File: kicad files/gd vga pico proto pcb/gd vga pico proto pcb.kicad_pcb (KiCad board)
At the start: 2 copper layers, 0 parts

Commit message: floor planning complete
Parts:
- added C1: 10u, Capacitor_SMD:C_0805_2012Metric, F.Cu at (88.2, 95.9)
- added C2: 1u, Capacitor_SMD:C_0805_2012Metric, B.Cu at (104.6, 79.2)
- added C3: 1u, Capacitor_SMD:C_0805_2012Metric, B.Cu at (103.1, 57.1)
- added C4: 1u, Capacitor_SMD:C_0805_2012Metric, B.Cu at (103.0, 68.7)
- added J1: RGB Bin, Connector_PinSocket_2.54mm:PinSocket_2x04_P2.54mm_Vertical, F.Cu at (80.1, 93.1)
- added J2: CLKS, Connector_PinSocket_2.54mm:PinSocket_2x04_P2.54mm_Vertical, F.Cu at (80.1, 49.6)
- added J3: Conn_01x05, Connector_PinHeader_2.54mm:PinHeader_1x05_P2.54mm_Vertical, F.Cu at (99.3, 46.1)
- added J4: L77HDE15SD1CH4F, Connector_Dsub:DSUB-15-HD_Female_Horizontal_P2.29x1.98mm_EdgePinOffset8.35mm_Housed_MountingHolesOffset10.89mm, F.Cu at (126.2, 68.7)
- added J5: VID_TXRX, Connector_PinHeader_2.54mm:PinHeader_1x04_P2.54mm_Vertical, F.Cu at (117.9, 64.7)
- added J6: WIN, Connector_PinHeader_2.54mm:PinHeader_1x02_P2.54mm_Vertical, F.Cu at (89.3, 79.4)
- added J7: 5V, Connector_PinSocket_2.54mm:PinSocket_1x04_P2.54mm_Vertical, F.Cu at (80.1, 63.4)
- added JP1: 14M, Jumper:SolderJumper-2_P1.3mm_Bridged_RoundedPad1.0x1.5mm, F.Cu at (84.3, 53.6)
- added JP2: 7M, Jumper:SolderJumper-2_P1.3mm_Open_TrianglePad1.0x1.5mm, F.Cu at (92.1, 46.5)
- added R1: 100, Resistor_SMD:R_0603_1608Metric, B.Cu at (127.7, 81.3)
- added R10: 100, Resistor_SMD:R_0603_1608Metric, B.Cu at (122.1, 77.7)
- added R11: 100, Resistor_SMD:R_0603_1608Metric, B.Cu at (122.1, 81.3)
- added R2: 1k, Resistor_SMD:R_0603_1608Metric, B.Cu at (117.7, 99.9)
- added R3: 390, Resistor_SMD:R_0603_1608Metric, B.Cu at (117.6, 97.4)
- added R4: 2k2, Resistor_SMD:R_0603_1608Metric, B.Cu at (117.8, 92.3)
- added R5: 1k, Resistor_SMD:R_0603_1608Metric, B.Cu at (117.8, 89.8)
- added R6: 470, Resistor_SMD:R_0603_1608Metric, B.Cu at (117.9, 87.2)
- added R7: 2k2, Resistor_SMD:R_0603_1608Metric, B.Cu at (117.8, 84.7)
- added R8: 1k, Resistor_SMD:R_0603_1608Metric, B.Cu at (117.5, 79.6)
- added R9: 470, Resistor_SMD:R_0603_1608Metric, B.Cu at (117.6, 77.1)
- added RNP1: 4k7, Resistor_SMD:R_0603_1608Metric, B.Cu at (121.9, 65.0)
- added RNP2: 4k7, Resistor_SMD:R_0603_1608Metric, B.Cu at (122.1, 62.0)
- added SW1: RESET, My Libraries:SW_Push_CK_PTS525_SM15, F.Cu at (92.7, 105.9)
- added TP1: TestPoint_Harwin, My Libraries:Harwin-S1751-46-Test-Point, F.Cu at (88.2, 90.0)
- added TP2: TestPoint_Harwin, My Libraries:Harwin-S1751-46-Test-Point, F.Cu at (122.1, 77.7)
- added TP3: TestPoint_Harwin, My Libraries:Harwin-S1751-46-Test-Point, F.Cu at (122.1, 81.1)
- added TP4: TestPoint_Harwin, My Libraries:Harwin-S1751-46-Test-Point, F.Cu at (124.7, 49.6)
- added TP5: TestPoint_Harwin, My Libraries:Harwin-S1751-46-Test-Point, F.Cu at (128.5, 94.2)
- added TP6: TestPoint_Harwin, My Libraries:Harwin-S1751-46-Test-Point, F.Cu at (122.0, 68.8)
- added TP7: TestPoint_Harwin, My Libraries:Harwin-S1751-46-Test-Point, F.Cu at (122.0, 71.1)
- added TP8: TestPoint_Harwin, My Libraries:Harwin-S1751-46-Test-Point, F.Cu at (122.0, 73.4)
- added U1: Pico, RPi_Pico:RPi_Pico_SMD_TH, F.Cu at (103.7, 75.8)
- added U2: 74HCT245, Package_SO:SO-20_5.3x12.6mm_P1.27mm, B.Cu at (104.9, 87.8)
- added U3: 74LVC2G04, Package_TO_SOT_SMD:SOT-23-6, B.Cu at (103.1, 60.3)
- added U4: 74LVC2G04, Package_TO_SOT_SMD:SOT-23-6, B.Cu at (103.1, 64.7)
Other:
- board outline added: 66 x 66 mm

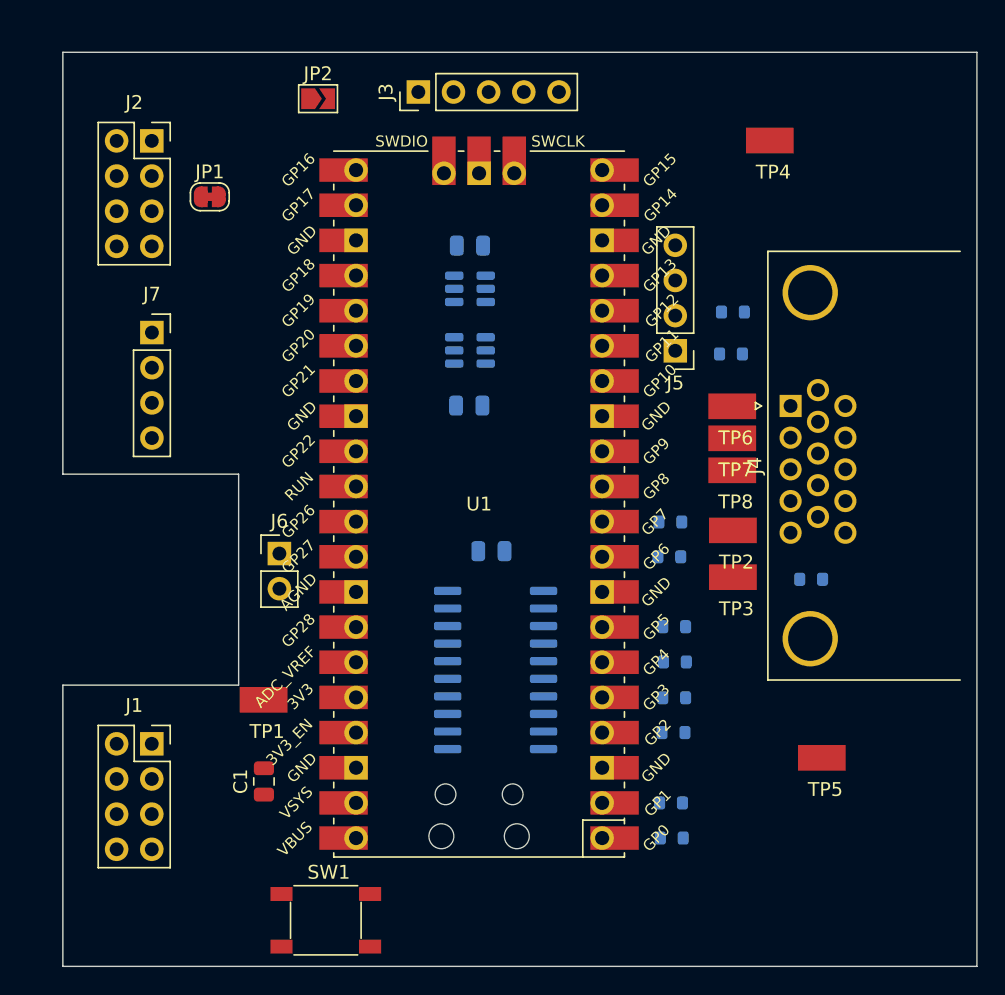
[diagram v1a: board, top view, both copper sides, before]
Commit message: swapped from pico to RP2040--yay
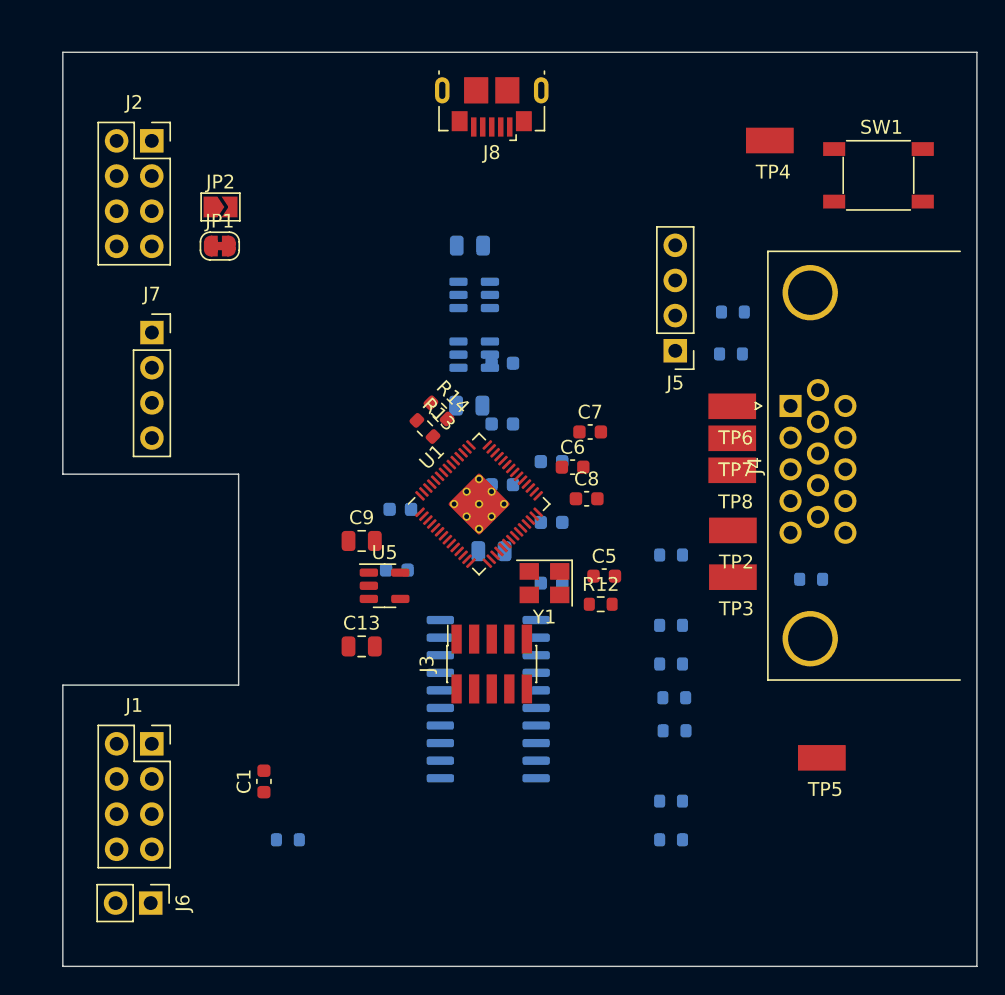
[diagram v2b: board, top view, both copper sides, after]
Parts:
- removed TP1: TestPoint_Harwin, My Libraries:Harwin-S1751-46-Test-Point
- added C10: 100n, Capacitor_SMD:C_0603_1608Metric, B.Cu at (105.4, 65.6)
- added C11: 1u, Capacitor_SMD:C_0603_1608Metric, B.Cu at (105.4, 70.0)
- added C12: 100n, Capacitor_SMD:C_0603_1608Metric, B.Cu at (105.4, 74.4)
- added C13: 1u, Capacitor_SMD:C_0805_2012Metric, F.Cu at (95.2, 86.1)
- added C14: 100n, Capacitor_SMD:C_0603_1608Metric, B.Cu at (109.0, 72.8)
- added C15: 100n, Capacitor_SMD:C_0603_1608Metric, B.Cu at (109.0, 77.1)
- added C16: 100n, Capacitor_SMD:C_0603_1608Metric, B.Cu at (109.0, 81.5)
- added C17: 100n, Capacitor_SMD:C_0603_1608Metric, B.Cu at (98.0, 76.2)
- added C18: 100n, Capacitor_SMD:C_0603_1608Metric, B.Cu at (97.8, 80.6)
- added C5: 27p, Capacitor_SMD:C_0603_1608Metric, F.Cu at (112.8, 81.0)
- added C6: 100n, Capacitor_SMD:C_0603_1608Metric, F.Cu at (110.5, 73.2)
- added C7: 100n, Capacitor_SMD:C_0603_1608Metric, F.Cu at (111.8, 70.6)
- added C8: 1u, Capacitor_SMD:C_0603_1608Metric, F.Cu at (111.5, 75.4)
- added C9: 1u, Capacitor_SMD:C_0805_2012Metric, F.Cu at (95.2, 78.5)
- added J8: USB_B_Micro, Connector_USB:USB_Micro-B_GCT_USB3076-30-A, F.Cu at (104.6, 47.1)
- added R12: 0, Resistor_SMD:R_0603_1608Metric, F.Cu at (112.5, 83.1)
- added R13: 27, Resistor_SMD:R_0603_1608Metric, F.Cu at (99.8, 70.4)
- added R14: 27, Resistor_SMD:R_0603_1608Metric, F.Cu at (100.8, 69.1)
- added U5: MIC5504-3.3YM5, Package_TO_SOT_SMD:SOT-23-5, F.Cu at (96.9, 81.7)
- added Y1: ECS-120-18-33-JEM-TR, Crystal:Crystal_SMD_3225-4Pin_3.2x2.5mm, F.Cu at (108.5, 81.5)
- C1: value 10u -> 27p; footprint Capacitor_SMD:C_0805_2012Metric -> Capacitor_SMD:C_0603_1608Metric
- J3: value Conn_01x05 -> SWD; footprint Connector_PinHeader_2.54mm:PinHeader_1x05_P2.54mm_Vertical -> Connector_PinSocket_1.27mm:PinSocket_2x05_P1.27mm_Vertical_SMD
- SW1: value RESET -> 2040 RESET
- U1: value Pico -> RP2040; footprint RPi_Pico:RPi_Pico_SMD_TH -> RP2040_minimal:RP2040-QFN-56
- moved SW1 67.0 mm to (132.6, 52.1)
- moved J3 41.7 mm to (104.6, 87.4)
- moved R9 35.9 mm to (89.9, 100.1), turned to 0 degrees
- moved J6 26.9 mm to (80.0, 104.6), turned to -90 degrees
- moved R8 20.4 mm to (117.6, 100.1)
- moved R2 20.4 mm to (117.6, 79.5)
- moved R3 12.8 mm to (117.6, 84.6)
- moved R7 12.6 mm to (117.6, 97.3)
- moved JP2 10.5 mm to (85.1, 54.4)
- moved R6 4.98 mm to (117.9, 92.2)
- moved R4 4.96 mm to (117.6, 87.4)
- moved JP1 3.63 mm to (85.0, 57.2)
- moved U2 2.17 mm to (104.4, 89.9), turned to 0 degrees
- moved U3 0.53 mm to (103.4, 60.7)
- moved U4 0.43 mm to (103.4, 65.0)
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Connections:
- C1 pad 1: +5V -> /XIN
- J3 pad 3: /SWCLK -> GND
- J3 pad 4: /RUN -> /SWCLK
- SW1 pad 1: /RUN -> GND
- SW1 pad 2: GND -> /VID_EN
- U1 pad 1: /RED0 -> +3V3
- U1 pad 10: /BLU2 -> +3V3
- U1 pad 13: GND -> unconnected-(U1-Pad13)
- U1 pad 14: /GPIO10 -> unconnected-(U1-Pad14)
- U1 pad 15: /VIN_EN -> unconnected-(U1-Pad15)
- U1 pad 16: /VID_TX -> unconnected-(U1-Pad16)
- U1 pad 17: /VID_RX -> /VGA_SDA
- U1 pad 18: GND -> /VGA_SCL
- U1 pad 19: /~{SYNC_RP} -> GND
- U1 pad 2: /RED1 -> /RED0
- U1 pad 20: /~{WINDOW_RP} -> /XIN
- U1 pad 21: /7M_RP -> /XOUT
- U1 pad 22: /14M_RP -> +3V3
- U1 pad 23: GND -> +1V1
- U1 pad 24: /RGB1_RP -> /SWCLK
- U1 pad 25: /RGB2_RP -> /SWDIO
- U1 pad 26: /RGB4_RP -> /VID_EN
- U1 pad 27: /RGB8_RP -> /VID_TX
- U1 pad 28: GND -> /VID_RX
- U1 pad 29: /SERVID_RP -> /~{WINDOW_RP}
- U1 pad 3: GND -> /RED1
- U1 pad 30: /RUN -> /~{SYNC_RP}
- U1 pad 31: /VGA_SDA -> /7M_RP
- U1 pad 32: /VGA_SCL -> /14M_RP
- U1 pad 33: GND -> +3V3
- U1 pad 34: /~{RESET_RP} -> /RGB1_RP
- U1 pad 35: unconnected-(U1-Pad35) -> /RGB2_RP
- U1 pad 36: +3V3 -> /RGB4_RP
- U1 pad 37: unconnected-(U1-Pad37) -> /RGB8_RP
- U1 pad 38: GND -> /SERVID_RP
- U1 pad 39: +5V -> unconnected-(U1-Pad39)
- U1 pad 40: VBUS -> unconnected-(U1-Pad40)
- U1 pad 41: /SWCLK -> unconnected-(U1-Pad41)
- U1 pad 42: GND -> +3V3
- U1 pad 43: /SWDIO -> +3V3
- U1 pad 8: GND -> /BLU1
- U1 pad 9: /BLU1 -> /BLU2

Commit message: post stream pixel pushing.
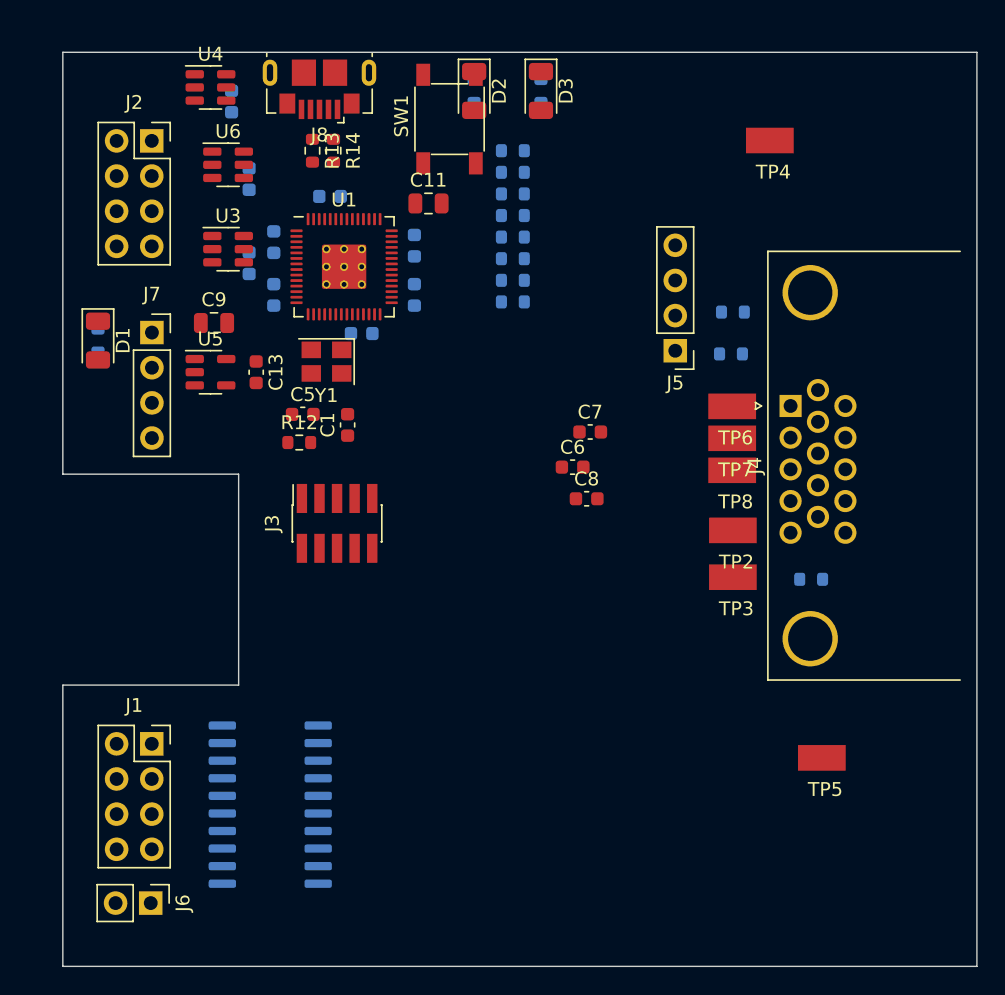
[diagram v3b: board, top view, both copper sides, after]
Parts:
- removed C18: 100n, Capacitor_SMD:C_0603_1608Metric
- removed JP1: 14M, Jumper:SolderJumper-2_P1.3mm_Bridged_RoundedPad1.0x1.5mm
- removed JP2: 7M, Jumper:SolderJumper-2_P1.3mm_Open_TrianglePad1.0x1.5mm
- added D1: 5V, LED_SMD:LED_1206_3216Metric, F.Cu at (76.2, 64.0)
- added D2: 3V, LED_SMD:LED_1206_3216Metric, F.Cu at (103.4, 46.0)
- added D3: L, LED_SMD:LED_1206_3216Metric, F.Cu at (108.2, 46.0)
- added R15: 1k, Resistor_SMD:R_0603_1608Metric, B.Cu at (76.2, 64.0)
- added R16: 1k, Resistor_SMD:R_0603_1608Metric, B.Cu at (103.4, 46.0)
- added R17: 1k, Resistor_SMD:R_0603_1608Metric, B.Cu at (108.2, 46.0)
- added U6: 74LVC2G04-DNP, Package_TO_SOT_SMD:SOT-23-6, F.Cu at (85.6, 51.3)
- C10, C12, C14, C15, C16: value 100n -> 1u
- C11: value 1u -> 10u; footprint Capacitor_SMD:C_0603_1608Metric -> Capacitor_SMD:C_0805_2012Metric; moved to F.Cu
- C13, C2: footprint Capacitor_SMD:C_0805_2012Metric -> Capacitor_SMD:C_0603_1608Metric
- C3, C4: value 1u -> 100n; footprint Capacitor_SMD:C_0805_2012Metric -> Capacitor_SMD:C_0603_1608Metric
- C9: value 1u -> 10u
- U3, U4: moved to F.Cu
- moved R9 43.6 mm to (106.2, 59.7)
- moved R7 40.8 mm to (106.2, 58.1)
- moved R8 40.5 mm to (106.2, 61.2)
- moved R6 37.5 mm to (106.2, 56.5)
- moved R5 36.7 mm to (106.2, 55.0)
- moved R4 35.8 mm to (106.2, 53.4)
- moved R3 34.7 mm to (106.2, 51.9)
- moved R2 31.4 mm to (106.2, 50.3)
- moved SW1 31.3 mm to (101.6, 48.0), turned to 90 degrees
- moved C15 28.5 mm to (88.9, 56.9), turned to -90 degrees
- moved C4 27.9 mm to (85.9, 46.7), turned to -90 degrees
- moved U4 27.1 mm to (84.3, 45.7), turned to 0 degrees
- moved C1 26.5 mm to (94.2, 70.1)
- moved C16 26.3 mm to (99.1, 57.1), turned to -90 degrees
- moved C17 26.2 mm to (87.1, 52.3), turned to -90 degrees
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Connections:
- U1 pad 13: unconnected-(U1-Pad13) -> /LED_L
- U2 pad 11: /7M_RP -> unconnected-(U2-Pad11)
- U2 pad 12: /14M_RP -> /~{WINDOW_RP}
- U2 pad 13: /~{WINDOW_RP} -> /~{SYNC_RP}
- U2 pad 14: /~{SYNC_RP} -> /RGB4_RP
- U2 pad 15: /RGB1_RP -> /RGB8_RP
- U2 pad 16: /RGB2_RP -> /RGB1_RP
- U2 pad 17: /RGB4_RP -> /RGB2_RP
- U2 pad 18: /RGB8_RP -> /SERVID_RP
- U2 pad 2: /RGB8 -> /SERVIDEO
- U2 pad 3: /RGB4 -> /RGB2
- U2 pad 4: /RGB2 -> /RGB8
- U2 pad 6: /~{SYNC} -> /RGB4
- U2 pad 7: /~{WINDOW} -> /~{SYNC}
- U2 pad 8: /7M_J -> /~{WINDOW}
- U2 pad 9: /14M_J -> GND
- U3 pad 1: /SERVIDEO -> /14M
- U3 pad 4: /SERVID_RP -> /14M_RP
- U3 pad 5: +3.3V -> +3V3
- U4 pad 5: +3.3V -> +3V3

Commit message: rev1 finish from stream, need final review
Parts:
- removed C15: 1u, Capacitor_SMD:C_0603_1608Metric
- removed C7: 100n, Capacitor_SMD:C_0603_1608Metric
- added C18: 100n, Capacitor_SMD:C_0805_2012Metric, B.Cu at (105.0, 55.7)
- added REF**: OSHW-Symbol_6.7x6mm_SilkScreen, Symbol:OSHW-Symbol_6.7x6mm_SilkScreen, F.Cu at (101.2, 78.3)
- added REF**: OSHW-Symbol_6.7x6mm_SilkScreen, Symbol:OSHW-Symbol_6.7x6mm_SilkScreen, B.Cu at (107.9, 95.6)
- added U7: W25Q128JVS, Package_SO:SOIC-8_5.23x5.23mm_P1.27mm, B.Cu at (101.6, 53.3)
- added kibuzzard-62146889: G***, kibuzzard-62146889, F.Cu at (79.8, 100.8)
- added kibuzzard-62146889: G***, kibuzzard-62146889, B.Cu at (79.8, 100.8)
- added kibuzzard-621468FD: G***, kibuzzard-621468FD, F.Cu at (81.3, 69.6)
- added kibuzzard-621468FD: G***, kibuzzard-621468FD, B.Cu at (81.3, 69.6)
- added kibuzzard-621469E6: G***, kibuzzard-621469E6, F.Cu at (78.9, 59.5)
- added kibuzzard-621469E6: G***, kibuzzard-621469E6, F.Cu at (99.7, 45.3)
- added kibuzzard-621469E6: G***, kibuzzard-621469E6, B.Cu at (99.7, 45.4)
- added kibuzzard-621469E6: G***, kibuzzard-621469E6, B.Cu at (78.8, 59.4)
- C1, C5: value 27p -> 6p; footprint Capacitor_SMD:C_0603_1608Metric -> Capacitor_SMD:C_0402_1005Metric
- C2, R15, R16, R17, R2, R3, R4, R5, R6, R7, R8, R9: moved to F.Cu
- C6: value 100n -> 1u; moved to B.Cu
- C8: moved to B.Cu
- J3: footprint Connector_PinSocket_1.27mm:PinSocket_2x05_P1.27mm_Vertical_SMD -> FTSH-105-01-L-DV-K:SAMTEC_FTSH-105-XX-X-DV
- J4: footprint Connector_Dsub:DSUB-15-HD_Female_Horizontal_P2.29x1.98mm_EdgePinOffset8.35mm_Housed_MountingHolesOffset10.89mm -> L77HDE15SD1CH4F:AMPHENOL_L77HDE15SD1CH4F
- Y1: value ECS-120-18-33-JEM-TR -> ABM10AIG-12.000MHZ-7-D2Z-T; footprint Crystal:Crystal_SMD_3225-4Pin_3.2x2.5mm -> Crystal:Crystal_SMD_2520-4Pin_2.5x2.0mm
- moved TP4 52.5 mm to (76.7, 70.7), turned to 90 degrees
- moved C2 43.2 mm to (90.2, 103.9)
- moved D2 40.0 mm to (88.9, 83.3), turned to 0 degrees
- moved R16 36.6 mm to (90.4, 80.2)
- moved TP8 30.3 mm to (94.4, 85.8)
- moved TP3 30.0 mm to (94.4, 92.8)
- moved TP2 30.0 mm to (94.4, 89.3)
- moved J3 29.9 mm to (92.6, 47.3), turned to 180 degrees
- moved TP7 29.8 mm to (94.4, 82.3)
- moved TP6 29.4 mm to (94.4, 78.7)
- moved J4 28.7 mm to (102.3, 84.7)
- moved R1 27.8 mm to (102.1, 91.9)
- moved RNP2 25.1 mm to (100.8, 75.4)
- moved RNP1 24.3 mm to (100.8, 76.9)
- moved C8 22.3 mm to (94.3, 61.2), turned to 45 degrees
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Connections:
- J5 pad 1: /VIN_EN -> /VID_EN
- U1 pad 11: /HSYNC -> unconnected-(U1-Pad11)
- U1 pad 12: /VSYNC -> unconnected-(U1-Pad12)
- U1 pad 13: /LED_L -> /~{RESET_RP}
- U1 pad 14: unconnected-(U1-Pad14) -> /SERVID_RP
- U1 pad 15: unconnected-(U1-Pad15) -> /7M_RP
- U1 pad 16: unconnected-(U1-Pad16) -> /14M_RP
- U1 pad 17: /VGA_SDA -> /RGB2_RP
- U1 pad 18: /VGA_SCL -> /RGB1_RP
- U1 pad 2: /RED0 -> unconnected-(U1-Pad2)
- U1 pad 27: /VID_TX -> /RGB8_RP
- U1 pad 28: /VID_RX -> /RGB4_RP
- U1 pad 29: /~{WINDOW_RP} -> /~{SYNC_RP}
- U1 pad 3: /RED1 -> unconnected-(U1-Pad3)
- U1 pad 30: /~{SYNC_RP} -> /~{WINDOW_RP}
- U1 pad 31: /7M_RP -> /VSYNC
- U1 pad 32: /14M_RP -> /HSYNC
- U1 pad 34: /RGB1_RP -> /BLU2
- U1 pad 35: /RGB2_RP -> /BLU1
- U1 pad 36: /RGB4_RP -> /BLU0
- U1 pad 37: /RGB8_RP -> /GRN2
- U1 pad 38: /SERVID_RP -> /GRN1
- U1 pad 39: unconnected-(U1-Pad39) -> /GRN0
- U1 pad 4: /GRN0 -> unconnected-(U1-Pad4)
- U1 pad 40: unconnected-(U1-Pad40) -> /RED1
- U1 pad 41: unconnected-(U1-Pad41) -> /RED0
- U1 pad 5: /GRN1 -> /LED_L
- U1 pad 6: /GRN2 -> /VID_TX
- U1 pad 7: /BLU0 -> /VID_RX
- U1 pad 8: /BLU1 -> unconnected-(U1-Pad8)
- U1 pad 9: /BLU2 -> unconnected-(U1-Pad9)
- U2 pad 1: +5V -> +3V3
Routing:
- net +3V3: track 0.00 -> 81.0 mm, vias 0 -> 23
- net /VID_EN: track 0.00 -> 80.5 mm, vias 0 -> 3
- net /SWDIO: track 0.00 -> 61.0 mm
- net /SWCLK: track 0.00 -> 58.4 mm
- net /VSYNC: track 0.00 -> 55.9 mm, vias 0 -> 2
- net /HSYNC: track 0.00 -> 52.7 mm, vias 0 -> 2
- net /SERVID_RP: track 0.00 -> 51.8 mm, vias 0 -> 1
- net /RGB2_RP: track 0.00 -> 50.7 mm, vias 0 -> 1
- net /RGB1_RP: track 0.00 -> 48.3 mm, vias 0 -> 1
- net /~{RESET_RP}: track 0.00 -> 45.9 mm
- net +5V: track 0.00 -> 39.6 mm, vias 0 -> 1
- net /RGB8_RP: track 0.00 -> 38.5 mm, vias 0 -> 1
- net /RGB4_RP: track 0.00 -> 36.7 mm, vias 0 -> 1
- net /~{SYNC_RP}: track 0.00 -> 35.0 mm, vias 0 -> 1
- net /~{WINDOW_RP}: track 0.00 -> 33.9 mm, vias 0 -> 1
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- added copper zone on B.Cu, net +3V3
- added copper zone on F.Cu, net +3V3
- added copper zone on F.Cu, net +5V
- added copper zone on F.Cu, net /VGA_B
- added copper zone on F.Cu, net /VGA_G
- added copper zone on F.Cu, net /VGA_R
- added copper zone on F.Cu, net /XIN
- added copper zone on F.Cu, net /XOUT
- added copper zone on B.Cu, net GND
- added copper zone on F.Cu, net GND
- added copper zone on F.Cu, net Net-(C5-Pad1)
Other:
- board size 66 x 66 mm -> 37.1 x 63.8 mm
- rule pad_to_mask_clearance: 0 -> 0.0508
- board text added: "${board_name} rev ${REVISION}, ${ISSUE_DATE} @baldengineer"
- board text added: "1"
- board text added: "2"
- board text added: "3v3"
- board text added: "4"
- board text added: "5V"
- board text added: "8"
- board text added: "B"
- board text added: "G"
- board text added: "H"
- board text added: "L"
- board text added: "R"
- board text added: "RESET"
- board text added: "S"
- board text added: "SYNC"
- board text added: "V"

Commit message: final rev1 silk clean up, add schematic, and add readme
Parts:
- removed the REF** at (101.2, 78.3)
- added kibuzzard-62146889: G***, kibuzzard-62146889, B.Cu at (99.6, 90.3)
- added kibuzzard-621469E6: G***, kibuzzard-621469E6, F.Cu at (109.7, 104.9)
- added kibuzzard-621469E6: G***, kibuzzard-621469E6, B.Cu at (103.9, 77.9)
- moved SW1 0.31 mm to (102.6, 50.4)
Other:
- board text added: "+5V"
- board text added: "14M"
- board text added: "1M"
- board text added: "7M"
- board text added: "EN"
- board text added: "Q3"
- board text added: "RX"
- board text added: "TX"
